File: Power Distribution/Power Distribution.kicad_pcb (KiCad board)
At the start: 16 copper layers, 20.1 x 34.5 mm, 18 parts, among them IC5 APX803

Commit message: Updated PCB
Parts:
- removed C2, C3: 1uF, 0805-NO
- removed C4, C5, C6: 10uF, 0805-NO
- removed FID3, FID4: FIDUCIAL_1MM, FIDUCIAL_1MM
- removed IC5: APX803, SOT23
- removed LCD1: OLED 128x32, UG-2832HSWEG02_WRAPUNDER
- removed R2: 10K, 0805-NO
- removed R3: 390K, 0805-NO
- removed RPI1: RASPBERRYPI_2X3, RASPBERRYPI_2X3_THMSMT
- removed U$1: , ADAFRUIT_2.5MM
- removed U$3: , PCBFEAT-REV-040
- removed U$4: MOUNTINGHOLE3.0THIN, MOUNTINGHOLE_3.0_PLATEDTHIN
- removed U$8: , ADAFRUIT_TEXT_20MM
- added ?: , , F.Cu at (118.0, 81.5)
- added ?: , , F.Cu at (130.5, 90.0)
- added ?: , , F.Cu at (115.5, 81.5)
- added ?: , , F.Cu at (118.0, 79.0)
- added ?: , , F.Cu at (115.5, 79.0)
- added ?: , , F.Cu at (128.0, 90.0)
- added REF**: RES_ERA6ARW473V, 47k:RES_ERA6ARW473V, F.Cu at (118.0, 75.0)
- added REF**: , Adafruit 128x32 Pi OLED:RASPBERRYPI_2X3_THMSMT, F.Cu at (133.0, 58.0)
- added REF**: CAPC3225X280N, 47uF:CAPC3225X280N, F.Cu at (122.0, 75.0)
- added REF**: , Adafruit 128x32 Pi OLED:MOUNTINGHOLE_3.0_PLATEDTHIN, F.Cu at (133.0, 50.5)
- moved REF** 9.60 mm to (95.5, 79.5)
- moved REF** 8.32 mm to (122.2, 99.0)
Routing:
- net 3.3V: track 35.7 -> 0.00 mm, vias 1 -> 0
- net SCL: track 27.5 -> 0.00 mm, vias 1 -> 0
- net SDA: track 26.6 -> 0.00 mm, vias 1 -> 0
- net ~{OLED_RST}: track 11.1 -> 0.00 mm
- net N$2: track 11.0 -> 0.00 mm, vias 2 -> 0
- net N$4: track 11.0 -> 0.00 mm, vias 2 -> 0
- net (no net): track 183.9 -> 174.1 mm
- net N$6: track 5.73 -> 0.00 mm
- net +5V: track 5.59 -> 0.00 mm, vias 1 -> 0
- net N$7: track 5.29 -> 0.00 mm
- net N$5: track 5.25 -> 0.00 mm
- net N$1: track 5.20 -> 0.00 mm
- net N$3: track 4.87 -> 0.00 mm
- net GND: vias 2 -> 0
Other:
- board outline removed
- board text added: "B+"
- board text added: "B-"
- board text removed: "0.9" 128x32 OLED For Raspberry Pi I2C 0x3C"
- board text removed: "I2C Pi OLED"

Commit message: Updated the PCB
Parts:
- added REF**: MODULE_2472, IMU:MODULE_2472, F.Cu at (143.5, 79.0)
- REF**: value RES_ERA6ARW473V -> 47kΩ
- REF**: value Charging Board -> Charging Board TP4056
- REF**: value CAPC3225X280N -> 47uF
- REF**: value MODULE_SC1176 -> Raspberry Pi Zero 2w
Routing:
- net (no net): track 174.1 -> 365.7 mm
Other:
- board text added: "Battery"
- board text added: "OLED"
- board text added: "Power Button"

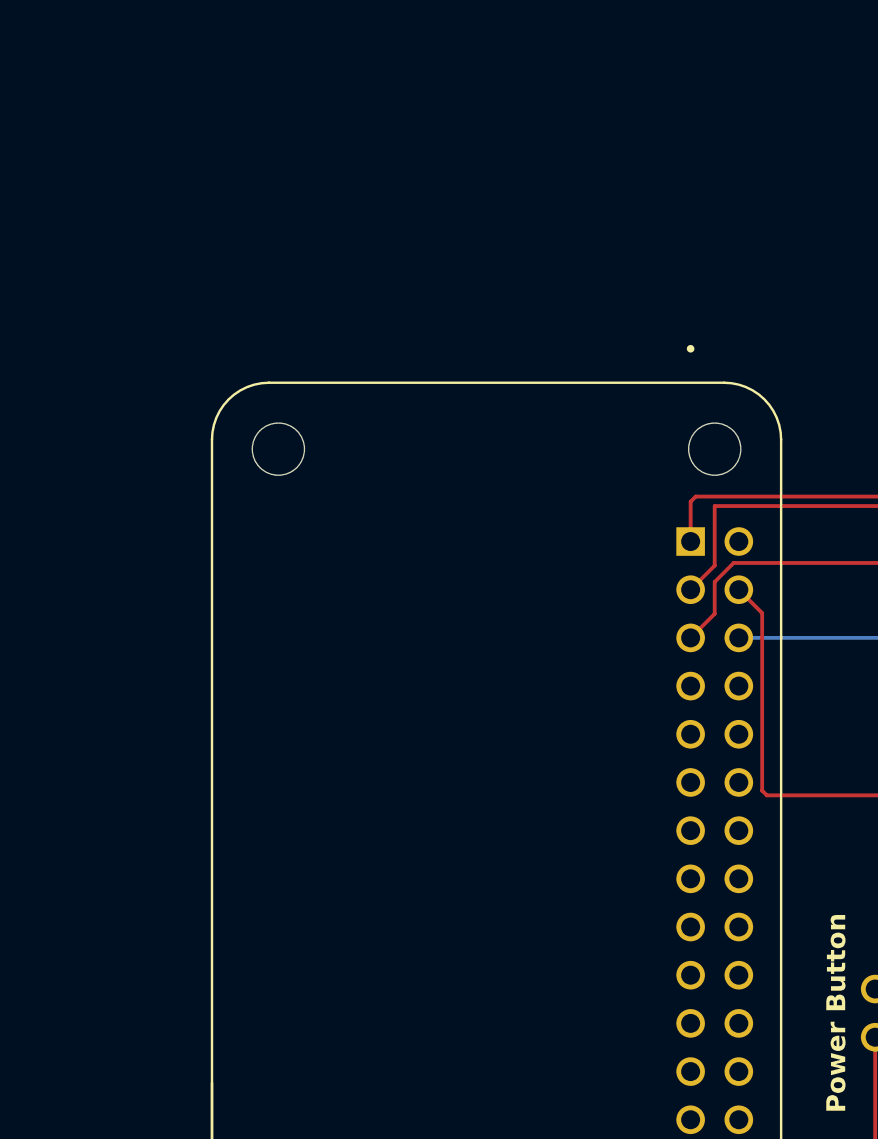
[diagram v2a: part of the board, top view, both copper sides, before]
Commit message: Finish adding the PCM5102a DAC Decoder
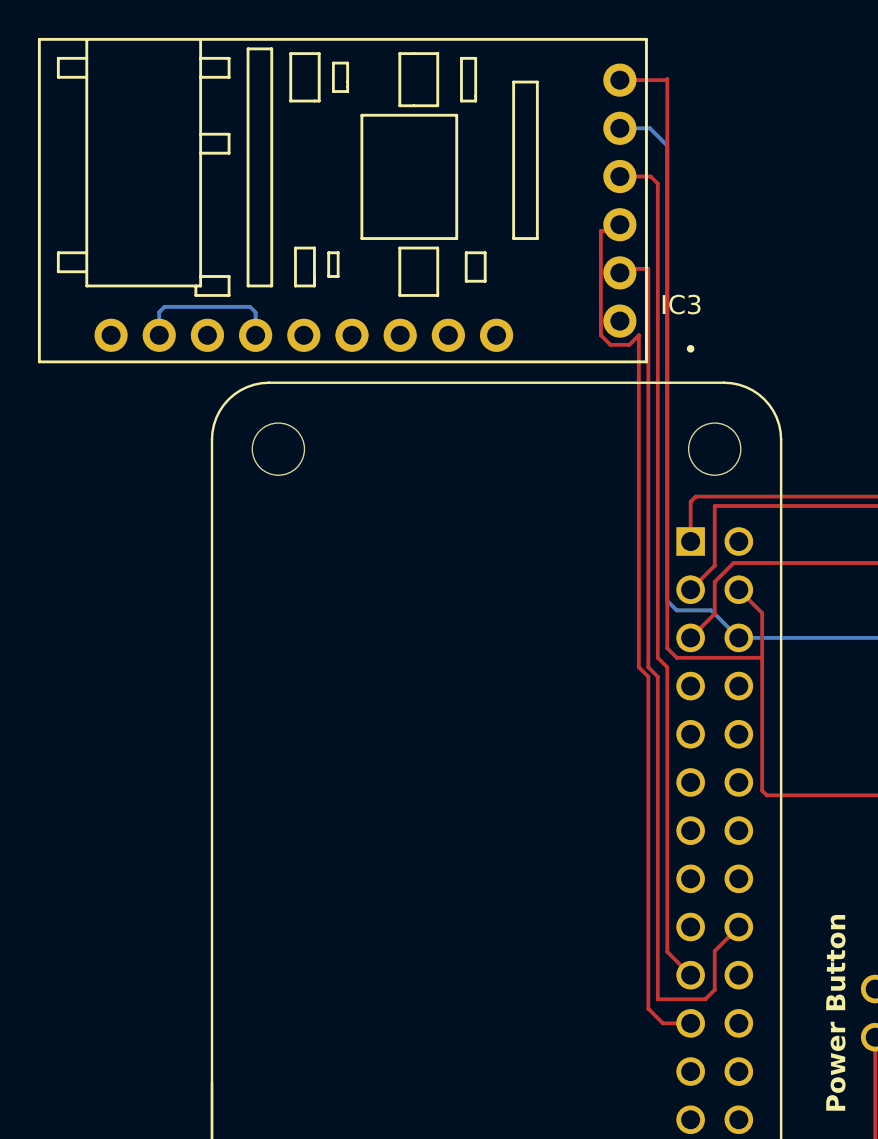
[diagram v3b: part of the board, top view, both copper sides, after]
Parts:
- added IC3: PCM5102 Audio Stereo DAC, PCM5102:PCM5102, F.Cu at (95.5, 44.5)
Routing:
- net (no net): track 365.7 -> 581.8 mm

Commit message: PCB updated
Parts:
- added ?: , , F.Cu at (115.0, 55.0)
- added ?: , , F.Cu at (112.5, 55.0)
- REF**: value MODULE_2472 -> IMU BNO055
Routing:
- net (no net): track 581.8 -> 591.5 mm
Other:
- board text added: "+"
- board text added: "-"
- board text added: "Camera"
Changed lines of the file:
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@@
+	(footprint ""
+		(layer "F.Cu")
+		(at 115 55 90)
+		(property "Reference" ""
+			(at 0 0 90)
+			(layer "F.SilkS")
+			(effects
+				(font
+					(size 1.27 1.27)
+					(thickness 0.15)
+				)
+			)
+		)
+		(property "Value" ""
+			(at 0 0 90)
+			(layer "F.Fab")
+			(effects
+				(font
+					(size 1.27 1.27)
+					(thickness 0.15)
+				)
+			)
+		)
+		(property "Datasheet" ""
+			(at 0 0 90)
+			(layer "F.Fab")
+			(hide yes)
+			(effects
+				(font
+					(size 1.27 1.27)
+					(thickness 0.15)
+				)
+			)
+		)
+		(property "Description" ""
+			(at 0 0 90)
+			(layer "F.Fab")
+			(hide yes)
+			(effects
+				(font
+					(size 1.27 1.27)
+					(thickness 0.15)
+				)
+			)
+		)
+		(pad "2" thru_hole circle
+			(at 0 0)
+			(size 1.508 1.508)
+			(drill 1)
+			(layers "*.Cu" "*.Mask")
+			(remove_unused_layers no)
+			(solder_mask_margin 0.102)
+		)
+		(embedded_fonts no)
+	)
 	(footprint ""
 		(layer "F.Cu")
@@
 			)
 		)
-		(property "Value" "MODULE_2472"
+		(property "Value" "IMU BNO055"
 			(at -6.6 12.045 90)
 			(layer "F.Fab")
@@
 		(pad "1" thru_hole circle
 			(at 0 0 270)
+			(size 1.508 1.508)
+			(drill 1)
+			(layers "*.Cu" "*.Mask")
+			(remove_unused_layers no)
+			(solder_mask_margin 0.102)
+		)
+		(embedded_fonts no)
+	)
+	(footprint ""
+		(layer "F.Cu")
+		(at 112.46 55 90)
+		(property "Reference" ""
+			(at 0 0 90)
+			(layer "F.SilkS")
+			(effects
+				(font
+					(size 1.27 1.27)
+					(thickness 0.15)
+				)
+			)
+		)
+		(property "Value" ""
+			(at 0 0 90)
+			(layer "F.Fab")
+			(effects
+				(font
+					(size 1.27 1.27)
+					(thickness 0.15)
+				)
+			)
+		)
+		(property "Datasheet" ""
+			(at 0 0 90)
+			(layer "F.Fab")
+			(hide yes)
+			(effects
+				(font
+					(size 1.27 1.27)
+					(thickness 0.15)
+				)
+			)
+		)
+		(property "Description" ""
+			(at 0 0 90)
+			(layer "F.Fab")
+			(hide yes)
+			(effects
+				(font
+					(size 1.27 1.27)
+					(thickness 0.15)
+				)
+			)
+		)
+		(pad "1" thru_hole circle
+			(at 0 0)
 			(size 1.508 1.508)
 			(drill 1)
@@
 		(embedded_fonts no)
 	)
-	(gr_text "B-\n"
-		(at 133 89 0)
-		(layer "B.Cu")
-		(effects
-			(font
-				(size 1.5 1.5)
-				(thickness 0.3)
-				(bold yes)
-			)
-			(justify left bottom mirror)
-		)
-	)
-	(gr_text "B+\n"
-		(at 128.5 89 0)
-		(layer "B.Cu")
-		(effects
-			(font
-				(size 1.5 1.5)
-				(thickness 0.3)
-				(bold yes)
-			)
-			(justify left bottom mirror)
-		)
-	)
 	(gr_text "Battery"
 		(at 132 85.5 180)
@@
 		)
 	)
+	(gr_text "Camera"
+		(at 116.5 57.5 0)
+		(layer "F.SilkS")
+		(effects
+			(font
+				(size 1 1)
+				(thickness 0.25)
+				(bold yes)
+			)
+			(justify left bottom mirror)
+		)
+	)
+	(gr_text "B-\n"
+		(at 133 89 0)
+		(layer "F.SilkS")
+		(effects
+			(font
+				(size 1.5 1.5)
+				(thickness 0.3)
+				(bold yes)
+			)
+			(justify left bottom mirror)
+		)
+	)
+	(gr_text "-"
+		(at 116 54 0)
+		(layer "F.SilkS")
+		(effects
+			(font
+				(size 1 1)
+				(thickness 0.25)
+				(bold yes)
+			)
+			(justify left bottom mirror)
+		)
+	)
+	(gr_text "+"
+		(at 113 54 0)
+		(layer "F.SilkS")
+		(effects
+			(font
+				(size 1 1)
+				(thickness 0.25)
+				(bold yes)
+			)
+			(justify left bottom mirror)
+		)
+	)
+	(gr_text "B+\n"
+		(at 128.5 89 0)
+		(layer "F.SilkS")
+		(effects
+			(font
+				(size 1.5 1.5)
+				(thickness 0.3)
+				(bold yes)
+			)
+			(justify left bottom mirror)
+		)
+	)
 	(segment
 		(start 104.5 62)
@@
 	)
 	(segment
+		(start 112.09 55.37)
+		(end 112.46 55)
+		(width 0.2)
+		(layer "F.Cu")
+		(net 0)
+	)
+	(segment
 		(start 108.27 75.69)
 		(end 107 76.96)
@@
 	)
 	(segment
-		(start 122 94.25)
-		(end 121.25 95)
-		(width 0.2)
-		(layer "F.Cu")
-		(net 0)
-	)
-	(segment
 		(start 131 59)
 		(end 131 59.81)
@@
 	)
 	(segment
-		(start 122 76.353)
-		(end 122 94.25)
-		(width 0.2)
-		(layer "F.Cu")
-		(net 0)
-	)
-	(segment
 		(start 104 36.5)
 		(end 103.63 36.13)
@@
 	)
 	(segment
+		(start 108.27 55.37)
+		(end 112.09 55.37)
+		(width 0.2)
+		(layer "F.Cu")
+		(net 0)
+	)
+	(segment
 		(start 104.5 61)
 		(end 104.5 31)
@@
 	)
 	(segment
+		(start 115 60.45)
+		(end 115 55)
+		(width 0.2)
+		(layer "B.Cu")
+		(net 0)
+	)
+	(segment
 		(start 78 43)
 		(end 82.5 43)
@@
 	(segment
 		(start 108.27 60.45)
-		(end 127.95 60.45)
+		(end 115 60.45)
+		(width 0.2)
+		(layer "B.Cu")
+		(net 0)
+	)
+	(segment
+		(start 121.25 95)
+		(end 121.25 77.25)
 		(width 0.2)
 		(layer "B.Cu")
@@
 	)
 	(segment
+		(start 121.25 77.25)
+		(end 122 76.5)
+		(width 0.2)
+		(layer "B.Cu")
+		(net 0)
+	)
+	(segment
 		(start 103.59 33.59)
 		(end 104.5 34.5)
@@
 		(width 0.2)
 		(layer "B.Cu")
+		(net 0)
+	)
+	(segment
+		(start 115 60.45)
+		(end 127.95 60.45)
+		(width 0.2)
+		(layer "B.Cu")

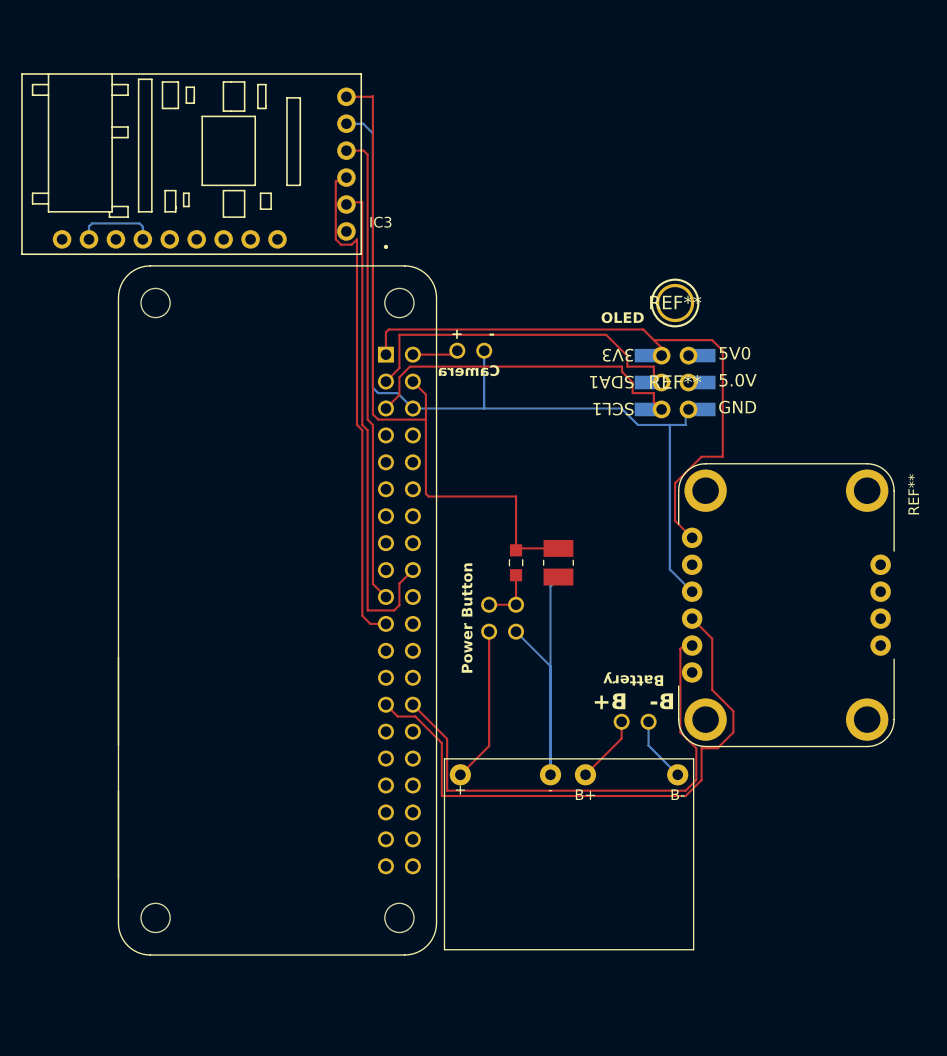
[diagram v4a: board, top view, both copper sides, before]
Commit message: added the speaker
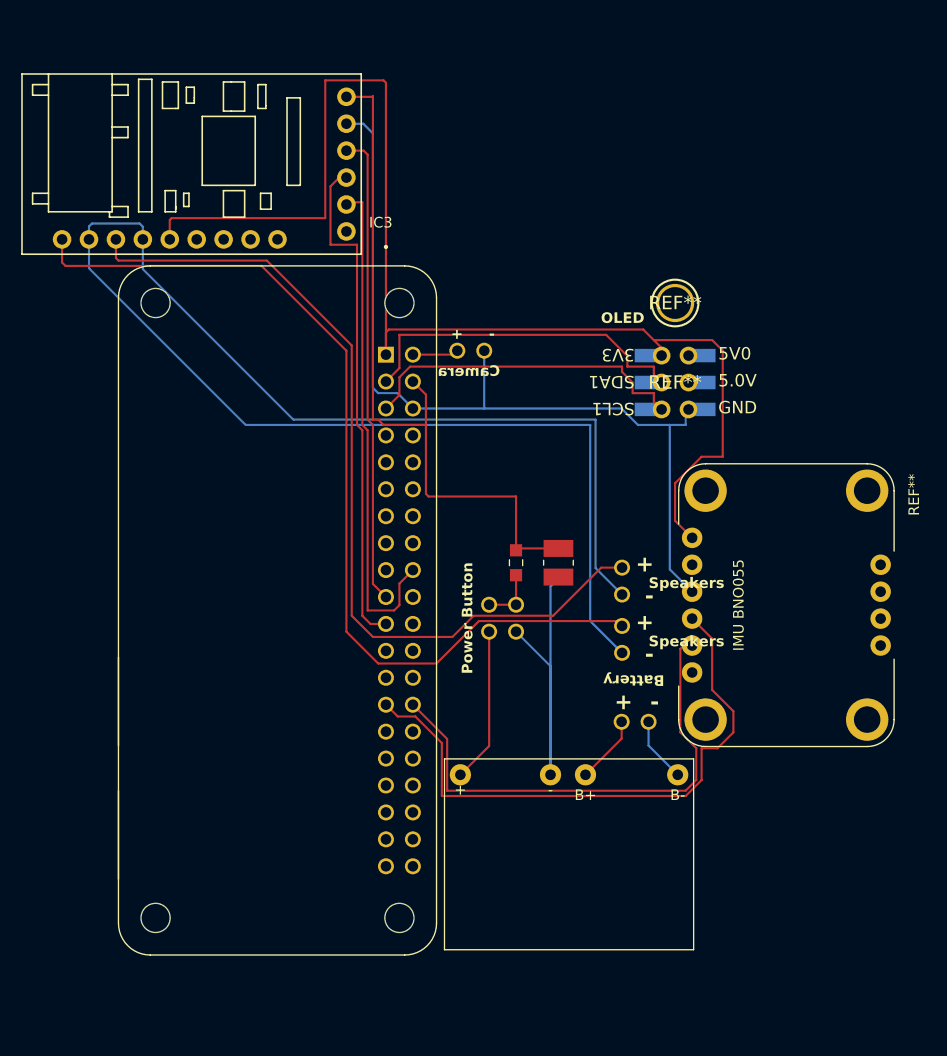
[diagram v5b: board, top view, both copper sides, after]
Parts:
- added ?: , , F.Cu at (128.0, 83.5)
- added ?: , , F.Cu at (128.0, 78.0)
- added ?: , , F.Cu at (128.0, 81.0)
- added ?: , , F.Cu at (128.0, 75.5)
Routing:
- net (no net): track 591.5 -> 971.5 mm
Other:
- board text added: "Speakers"
- board text removed: "B+"
- board text removed: "B-"

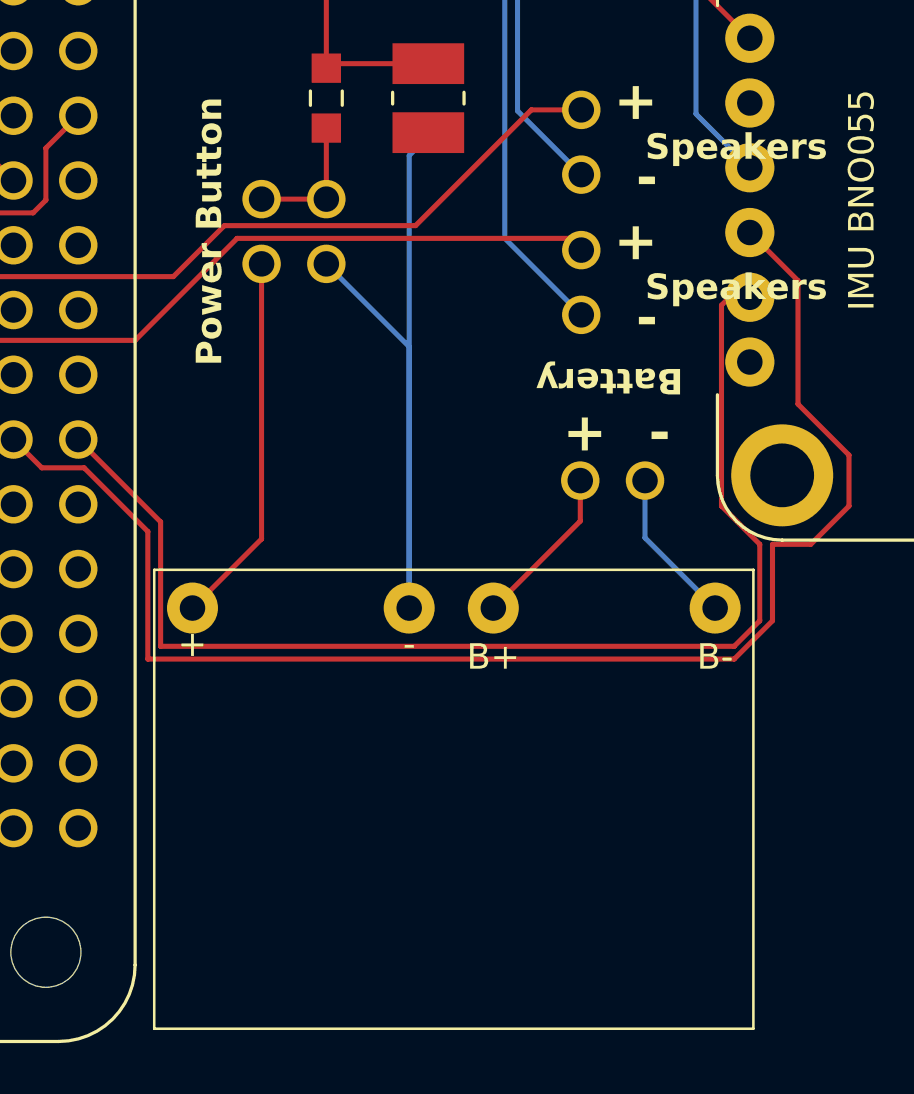
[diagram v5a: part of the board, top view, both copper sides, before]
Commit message: fix charging board
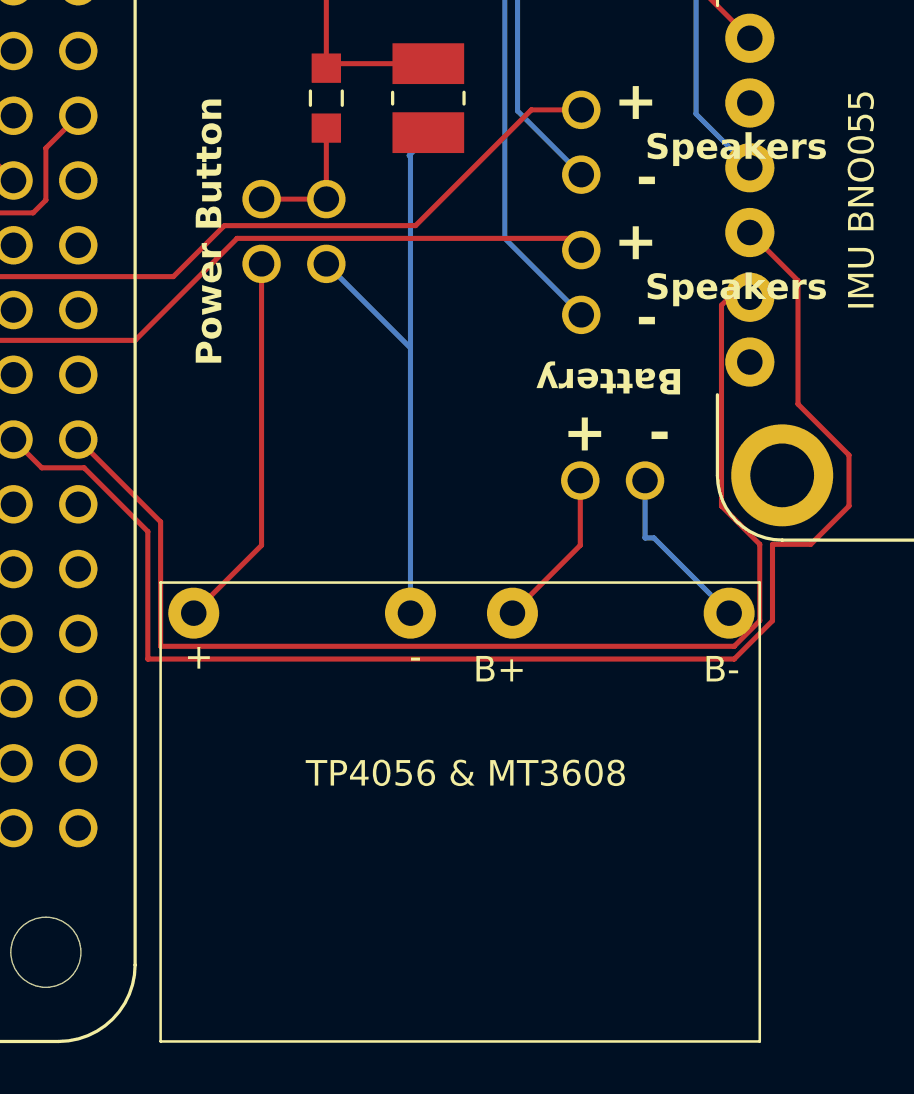
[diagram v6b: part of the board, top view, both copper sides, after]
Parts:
- removed the REF** at (122.2, 99.0)
- added TP4056 & MT3608: Charging Board, ChargingBoardTP4056:Charging Board TP4056, F.Cu at (122.5, 99.5)
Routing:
- net (no net): track 971.5 -> 962.3 mm
